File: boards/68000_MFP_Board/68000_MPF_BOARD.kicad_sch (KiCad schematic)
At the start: 25 parts, among them J1 Conn_01x08, J11 Conn_01x08, J13 Conn_01x10, J2 Conn_02x04_Odd_Even, J3 Conn_01x03, J4 Conn_02x10_Odd_Even, J5 Conn_02x05_Odd_Even, J6 Conn_02x02_Odd_Even, J7 Conn_01x06, J8 Conn_01x06, J9 Conn_01x08, M1 RC2014_40_PIN, U1 74LS138, U4 68901P, U5 68901P, X1 CXO_DIP8

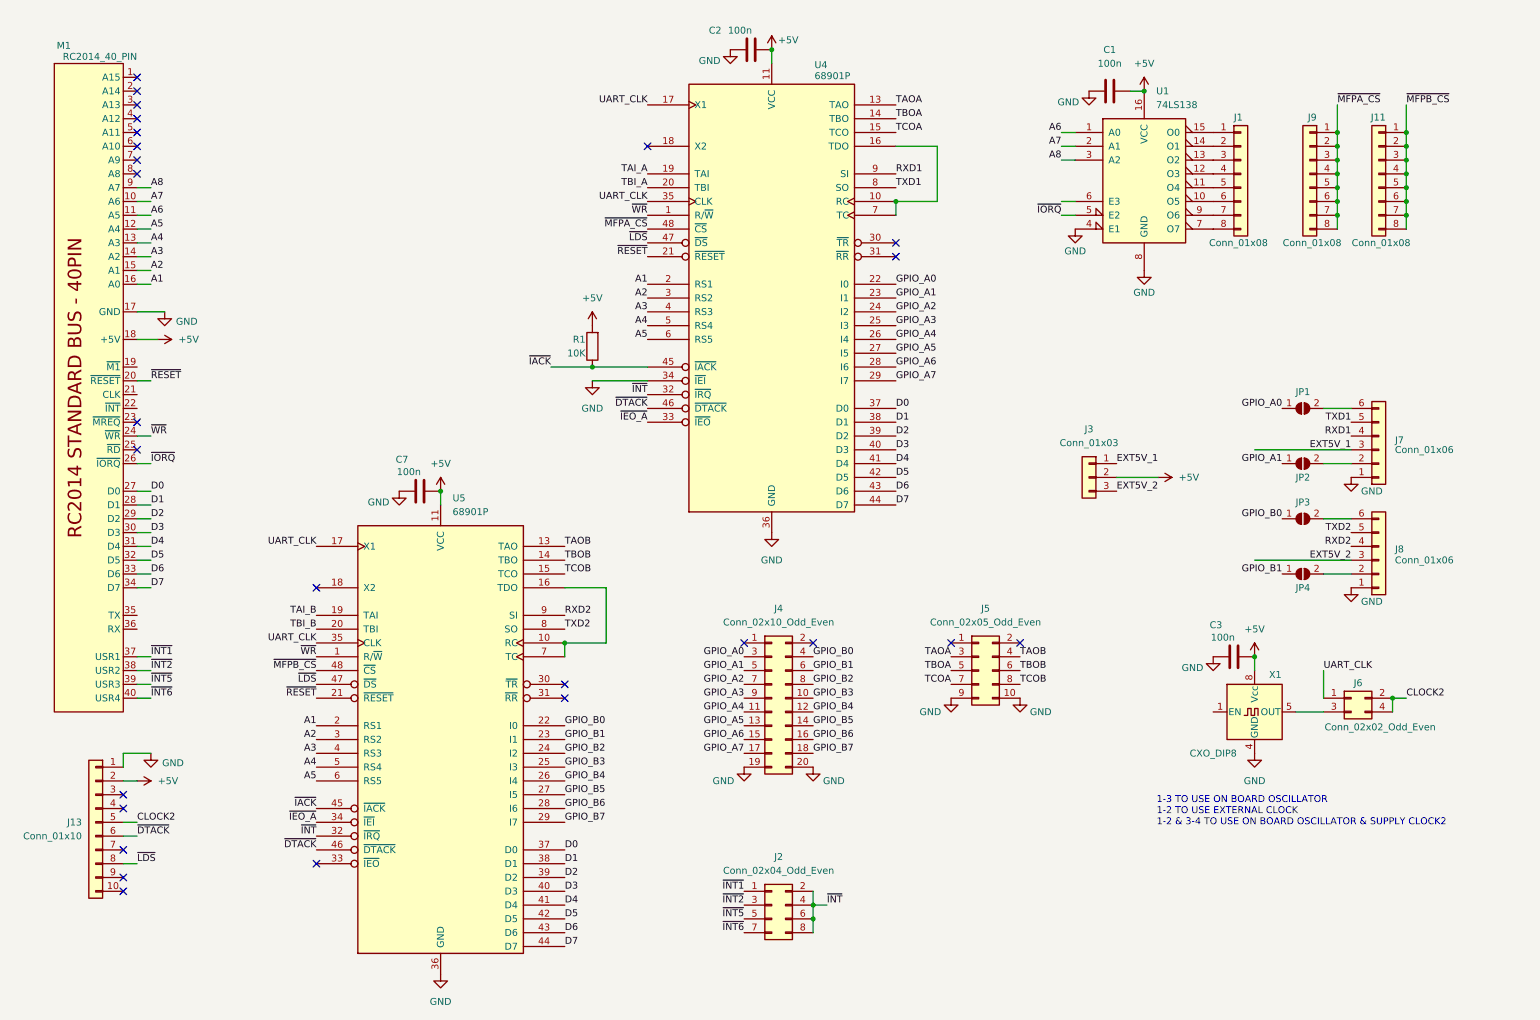
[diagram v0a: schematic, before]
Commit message: Update to v2 board set
Lots of updates to reflect the new v2 boards that use the full RCBus 80 pins as well as slight modifications to the various test programs to reflect the new IO and MEM space addresses.
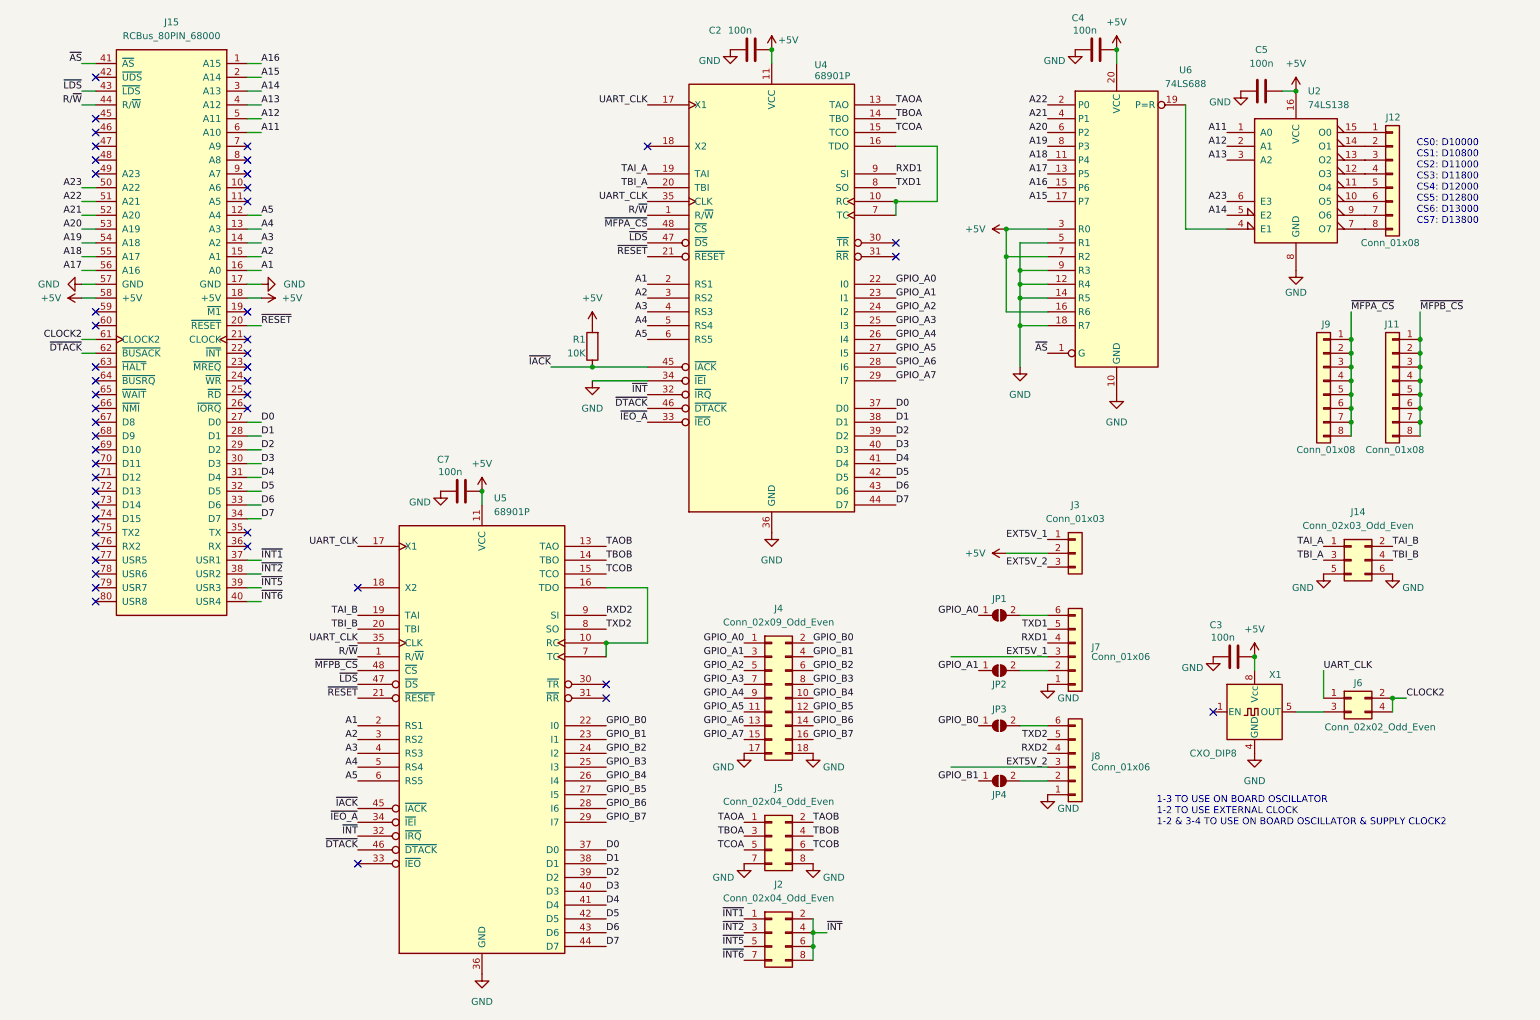
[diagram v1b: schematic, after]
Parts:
- removed C1: 100n, Capacitor_THT:C_Disc_D5.0mm_W2.5mm_P2.50mm, symbol Device:C
- removed J1: Conn_01x08, MyLibrary2023:PinHeader_1x08_P2.54mm_Vertical, symbol Connector_Generic:Conn_01x08
- removed J13: Conn_01x10, MyLibrary2023:PinHeader_1x10_P2.54mm_Vertical, symbol Connector_Generic:Conn_01x10
- removed J4: Conn_02x10_Odd_Even, Connector_PinHeader_2.54mm:PinHeader_2x10_P2.54mm_Horizontal, symbol Connector_Generic:Conn_02x10_Odd_Even
- removed J5: Conn_02x05_Odd_Even, Connector_PinHeader_2.54mm:PinHeader_2x05_P2.54mm_Horizontal, symbol Connector_Generic:Conn_02x05_Odd_Even
- removed M1: RC2014_40_PIN, MyLibrary2023:RC2014_STD_40_PIN, symbol MyLibrary2023:RC2014_40_PIN
- removed U1: 74LS138, Package_DIP:DIP-16_W7.62mm_Socket, symbol 74xx:74LS138
- added C4, C5: 100n, Capacitor_THT:C_Disc_D5.0mm_W2.5mm_P2.50mm, symbol Device:C
- added J12: Conn_01x08, MyLibrary2023:PinHeader_1x08_P2.54mm_Vertical, symbol Connector_Generic:Conn_01x08
- added J14: Conn_02x03_Odd_Even, Connector_PinHeader_2.54mm:PinHeader_2x03_P2.54mm_Vertical, symbol Connector_Generic:Conn_02x03_Odd_Even
- added J15: RCBus_80PIN_68000, MyLibrary2023:RCBus_80p_Medium, symbol MyLibrary2023:RCBus_80PIN_68000
- added J4: Conn_02x09_Odd_Even, Connector_PinHeader_2.54mm:PinHeader_2x09_P2.54mm_Vertical, symbol Connector_Generic:Conn_02x09_Odd_Even
- added J5: Conn_02x04_Odd_Even, Connector_PinHeader_2.54mm:PinHeader_2x04_P2.54mm_Vertical, symbol Connector_Generic:Conn_02x04_Odd_Even
- added U2: 74LS138, Package_DIP:DIP-16_W7.62mm_Socket, symbol 74xx:74LS138
- added U6: 74LS688, MyLibrary2023:DIP-20_W7.62mm_Socket, symbol 74xx:74LS688
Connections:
- net +5V: now also C4.2, C5.2, J15.18 (+5V), J15.58 (+5V), U2.16 (VCC), U6.16 (R6), U6.20 (VCC), U6.3 (R0), U6.7 (R2)
- net A1: now also J15.16 (A0)
- net A2: now also J15.15 (A1)
- net A3: now also J15.14 (A2)
- net A4: now also J15.13 (A3)
- net A5: now also J15.12 (A4)
- net CLOCK2: now also J15.61 (CLOCK2)
- net D0: now also J15.27 (D0)
- net D1: now also J15.28 (D1)
- net D2: now also J15.29 (D2)
- net D3: now also J15.30 (D3)
- net D4: now also J15.31 (D4)
- net D5: now also J15.32 (D5)
- net D6: now also J15.33 (D6)
- net D7: now also J15.34 (D7)
- net GND: now also C4.1, C5.1, J14.5 (Pin_5), J14.6 (Pin_6), J15.17 (GND), J15.57 (GND), J4.17 (Pin_17), J4.18 (Pin_18), J5.7 (Pin_7), J5.8 (Pin_8), U2.8 (GND), U6.10 (GND), U6.12 (R4), U6.14 (R5), U6.18 (R7), U6.5 (R1), U6.9 (R3)
- net GPIO_A0: now also J4.1 (Pin_1)
- net GPIO_A1: now also J4.3 (Pin_3)
- net GPIO_A2: now also J4.5 (Pin_5)
- net GPIO_A3: now also J4.7 (Pin_7)
- net GPIO_A4: now also J4.9 (Pin_9)
- net GPIO_A5: now also J4.11 (Pin_11)
- net GPIO_A6: now also J4.13 (Pin_13)
- net GPIO_A7: now also J4.15 (Pin_15)
- net GPIO_B0: now also J4.2 (Pin_2)
- net GPIO_B1: now also J4.4 (Pin_4)
- net GPIO_B2: now also J4.6 (Pin_6)
- net GPIO_B3: now also J4.8 (Pin_8)
- net GPIO_B4: now also J4.10 (Pin_10)
- net GPIO_B5: now also J4.12 (Pin_12)
- net GPIO_B6: now also J4.14 (Pin_14)
- net GPIO_B7: now also J4.16 (Pin_16)
- net TAI_A: now also J14.1 (Pin_1)
- net TAI_B: now also J14.2 (Pin_2)
- net TAOA: now also J5.1 (Pin_1)
- net TAOB: now also J5.2 (Pin_2)
- net TBI_A: now also J14.3 (Pin_3)
- net TBI_B: now also J14.4 (Pin_4)
- net TBOA: now also J5.3 (Pin_3)
- net TBOB: now also J5.4 (Pin_4)
- net TCOA: now also J5.5 (Pin_5)
- net TCOB: now also J5.6 (Pin_6)
- net ~{DTACK}: now also J15.62 (~{BUSACK})
- net ~{INT1}: now also J15.37 (USR1)
- net ~{INT2}: now also J15.38 (USR2)
- net ~{INT5}: now also J15.39 (USR3)
- net ~{INT6}: now also J15.40 (USR4)
- net ~{LDS}: now also J15.43 (~{LDS})
- net ~{RESET}: now also J15.20 (~{RESET})
- net ~{WR} renamed R/~{W}
- net R/~{W}: now also J15.44 (R/~{W})
- new net: J12.6 (Pin_6), U2.10 (O5)
- new net: J12.5 (Pin_5), U2.11 (O4)
- new net: J12.4 (Pin_4), U2.12 (O3)
- new net: J12.3 (Pin_3), U2.13 (O2)
- new net: J12.2 (Pin_2), U2.14 (O1)
- new net: J12.1 (Pin_1), U2.15 (O0)
- new net: U2.4 (E1), U6.19 (P=R)
- new net: J12.8 (Pin_8), U2.7 (O7)
- new net: J12.7 (Pin_7), U2.9 (O6)
- new net A11: J15.6 (A10), U2.1 (A0)
- new net A12: J15.5 (A11), U2.2 (A1)
- new net A13: J15.4 (A12), U2.3 (A2)
- new net A14: J15.3 (A13), U2.5 (E2)
- new net A15: J15.2 (A14), U6.17 (P7)
- new net A16: J15.1 (A15), U6.15 (P6)
- new net A17: J15.56 (A16), U6.13 (P5)
- new net A18: J15.55 (A17), U6.11 (P4)
- new net A19: J15.54 (A18), U6.8 (P3)
- new net A20: J15.53 (A19), U6.6 (P2)
- new net A21: J15.52 (A20), U6.4 (P1)
- new net A22: J15.51 (A21), U6.2 (P0)
- new net A23: J15.50 (A22), U2.6 (E3)
- new net ~{AS}: J15.41 (~{AS}), U6.1 (G)
- no-connect marks 26 -> 48
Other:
- note added: "CS0: D10000 CS1: D10800 CS2: D11000 CS3: D11800 CS4: D12000 CS5: D12800 CS6: D13000 CS7: D13800"
- moved on the sheet: C7, J11, J2, J3, J7, J8, J9, JP1, JP2, JP3, JP4, U5
